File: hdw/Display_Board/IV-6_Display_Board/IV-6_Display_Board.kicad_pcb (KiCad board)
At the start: 4 copper layers, 200 x 50 mm, 238 parts, among them J3001 DSP_IO_Connector, Q1101 PMSTA06, Q1102 BC856W, Q1103 PMSTA06, Q1104 BC856W, Q1105 PMSTA06, Q1106 BC856W, Q1107 PMSTA06, Q1108 BC856W, Q201 PMSTA06, Q202 PMSTA06, Q203 BC856W, Q204 BC856W, Q205 PMSTA06, Q206 PMSTA06, Q207 BC856W, Q208 BC856W, Q209 PMSTA06, Q210 PMSTA06, Q211 BC856W, Q212 BC856W, Q213 PMSTA06, Q214 PMSTA06, Q215 BC856W, Q216 BC856W, Q301 PMSTA06, Q302 PMSTA06, Q303 BC856W, Q304 BC856W, Q305 PMSTA06, Q306 PMSTA06, Q307 BC856W, Q308 BC856W, Q309 PMSTA06, Q310 PMSTA06, Q311 BC856W, Q312 BC856W, SW601 Cap_Touch, SW602 Cap_Touch, SW801 Cap_Touch, SW802 Cap_Touch, SW901 Cap_Touch, U1001 MCP9804, U1301 DS1683, U1302 LTC4316DD, U501 TCA9555RGER, U601 TLV71333PDBV, U602 TLV71333PDBV, U603 AT42QT1010-TSHR, U604 AT42QT1010-TSHR, U605 74LVC1G97, U606 74LVC1G97, U801 TLV71333PDBV, U802 TLV71333PDBV, U803 AT42QT1010-TSHR, U804 AT42QT1010-TSHR, U805 74LVC1G97, U806 74LVC1G97, U901 TLV71333PDBV, U902 AT42QT1010-TSHR, U903 74LVC1G97

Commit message: refactored a lot of display board stuff
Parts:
- Q1101, Q1102, Q1103, Q1104, Q1105, Q1106, Q1107, Q1108, Q301, Q302, Q303, Q304, Q305, Q306, Q307, Q308, Q309, Q310, Q311, Q312, R1101, R1102, R1103, R1104, R1105, R1106, R1107, R1108, R1109, R1110, R1111, R1112, R1113, R1114, R1115, R1116, R1117, R1118, R1119, R1120, R1121, R1122, R1123, R1124, R301, R302, R303, R304, R305, R306, R307, R308, R309, R310, R311, R312, R313, R314, R315, R316, R317, R318, R319, R320, R321, R322, R323, R324: moved to B.Cu
- R501, R502, R503, R504, R505, R506, R507, R508, R509, R510, R511: moved to F.Cu
- moved R229 122.8 mm to (227.4, 74.4), turned to 90 degrees
- moved Q214 119.9 mm to (224.8, 69.7), turned to 270 degrees
- moved R230 118.6 mm to (224.8, 72.2), turned to 180 degrees
- moved Q216 117.7 mm to (224.8, 74.4), turned to 180 degrees
- moved R226 116.0 mm to (222.6, 69.2), turned to 270 degrees
- moved R232 113.7 mm to (222.2, 72.2), turned to 90 degrees
- moved R221 108.2 mm to (220.1, 74.4), turned to 90 degrees
- moved C1301 106.6 mm to (280.2, 106.2)
- moved C1302 106.6 mm to (281.6, 106.2)
- moved C1303 106.6 mm to (283.0, 106.2)
- moved C1304 106.6 mm to (278.8, 106.2)
- moved C1305 106.6 mm to (287.4, 103.4)
- moved D1301 106.6 mm to (286.2, 106.9)
- moved R1303 106.6 mm to (287.4, 104.9)
- moved R1304 106.6 mm to (287.4, 103.4)
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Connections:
- Q203 pad 3: Anode_A_VFD -> Anode_G_VFD
- Q204 pad 3: Anode_E_VFD -> Anode_D_VFD
- Q207 pad 3: Anode_B_VFD -> Anode_E_VFD
- Q208 pad 3: Anode_F_VFD -> Anode_C_VFD
- Q211 pad 3: Anode_C_VFD -> Anode_DP_VFD
- Q212 pad 3: Anode_G_VFD -> Anode_B_VFD
- Q215 pad 3: Anode_D_VFD -> Anode_F_VFD
- Q216 pad 3: Anode_DP_VFD -> Anode_A_VFD
- R201 pad 1: Anode_A_DSP -> Anode_G_DSP
- R202 pad 1: Anode_E_DSP -> Anode_D_DSP
- R207 pad 1: Anode_A_VFD -> Anode_G_VFD
- R208 pad 1: Anode_E_VFD -> Anode_D_VFD
- R209 pad 1: Anode_B_DSP -> Anode_E_DSP
- R210 pad 1: Anode_F_DSP -> Anode_C_DSP
- R215 pad 1: Anode_B_VFD -> Anode_E_VFD
- R216 pad 1: Anode_F_VFD -> Anode_C_VFD
- R217 pad 1: Anode_C_DSP -> Anode_DP_DSP
- R218 pad 1: Anode_G_DSP -> Anode_B_DSP
- R223 pad 1: Anode_C_VFD -> Anode_DP_VFD
- R224 pad 1: Anode_G_VFD -> Anode_B_VFD
- R225 pad 1: Anode_D_DSP -> Anode_F_DSP
- R226 pad 1: Anode_DP_DSP -> Anode_A_DSP
- R231 pad 1: Anode_D_VFD -> Anode_F_VFD
- R232 pad 1: Anode_DP_VFD -> Anode_A_VFD
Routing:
- net Cap_Touch_Up_DSP: track 202.2 -> 0.00 mm, vias 8 -> 0
- net Grid_5_DSP: track 187.8 -> 0.00 mm, vias 3 -> 0
- net Cap_Touch_Down_DSP: track 181.4 -> 0.00 mm, vias 6 -> 0
- net Grid_4_DSP: track 165.4 -> 0.00 mm, vias 3 -> 0
- net Colon_0_DSP: track 153.5 -> 0.00 mm, vias 3 -> 0
- net Colon_1_DSP: track 131.2 -> 0.00 mm, vias 3 -> 0
- net Cap_Touch_Left_DSP: track 130.7 -> 0.00 mm, vias 4 -> 0
- net I2C_DSP_SCL: track 129.7 -> 0.00 mm, vias 3 -> 0
- net Grid_3_DSP: track 119.1 -> 0.00 mm, vias 3 -> 0
- net Cap_Touch_Right_DSP: track 111.8 -> 0.00 mm, vias 2 -> 0
- net Grid_2_DSP: track 96.5 -> 0.00 mm, vias 3 -> 0
- net I2C_DSP_SDA: track 90.1 -> 0.00 mm, vias 1 -> 0
- net Colon_2_DSP: track 87.7 -> 0.00 mm, vias 3 -> 0
- net Anode_B_DSP: track 102.3 -> 27.8 mm, vias 4 -> 2
- net Anode_A_DSP: track 89.8 -> 21.1 mm, vias 4 -> 2
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
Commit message: More display board fixes
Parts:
- added G***: LOGO, Custom Footprints Library:VFD_QR_Code, F.Cu at (139.6, 51.9)
- added G***: LOGO, Custom Footprints Library:VFD_CLock_Logo_Silk, F.Cu at (134.5, 70.4)
- moved U1001 98.5 mm to (197.8, 132.0), turned to 180 degrees
- moved C1001 98.0 mm to (197.8, 134.2), turned to 0 degrees
- moved U1302 69.6 mm to (221.9, 123.5), turned to 180 degrees
- moved C1305 65.5 mm to (225.0, 123.5), turned to 270 degrees
- moved R1304 65.5 mm to (225.0, 123.5), turned to 270 degrees
- moved R1303 63.6 mm to (226.6, 123.5), turned to 90 degrees
- moved D1301 60.3 mm to (228.6, 124.7), turned to 90 degrees
- moved U1301 60.2 mm to (226.6, 129.2), turned to 270 degrees
- moved R1301 60.0 mm to (225.2, 133.8), turned to 180 degrees
- moved C1303 59.3 mm to (227.8, 127.9), turned to 180 degrees
- moved C1302 58.5 mm to (227.8, 129.3), turned to 180 degrees
- moved C1301 57.8 mm to (227.8, 130.7), turned to 180 degrees
- moved R1302 57.8 mm to (226.9, 133.8), turned to 180 degrees
- moved C1304 57.2 mm to (227.8, 132.1), turned to 180 degrees
- moved Q306 2.45 mm to (200.7, 94.8)
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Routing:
- net Grid_0_DSP: track 0.00 -> 27.5 mm, vias 0 -> 2
- net Grid_1_DSP: track 0.00 -> 26.6 mm, vias 0 -> 2
- net Grid_2_DSP: track 0.00 -> 25.7 mm, vias 0 -> 2
- net Grid_3_DSP: track 0.00 -> 24.8 mm, vias 0 -> 2
- net Grid_4_DSP: track 0.00 -> 23.9 mm, vias 0 -> 2
- net Grid_5_DSP: track 0.00 -> 23.1 mm, vias 0 -> 2
- net Colon_0_DSP: track 0.00 -> 22.2 mm, vias 0 -> 2
- net Colon_1_DSP: track 0.00 -> 21.3 mm, vias 0 -> 2
- net Colon_2_DSP: track 0.00 -> 20.6 mm, vias 0 -> 2
- net Colon_3_DSP: track 0.00 -> 20.0 mm, vias 0 -> 2
- net Net-(Q306-Pad3): track 1.85 -> 3.79 mm

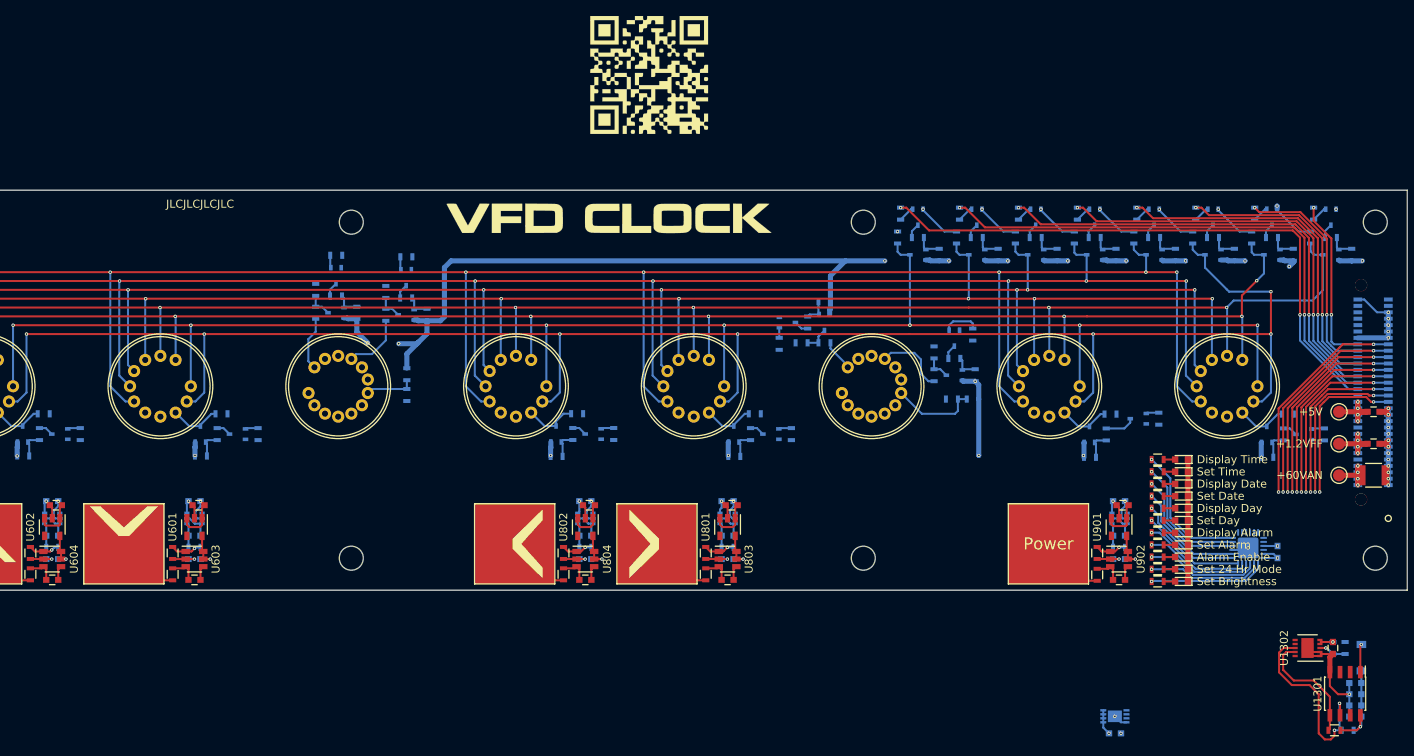
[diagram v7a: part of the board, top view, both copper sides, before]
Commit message: reclassed some nets, placed I2C devices
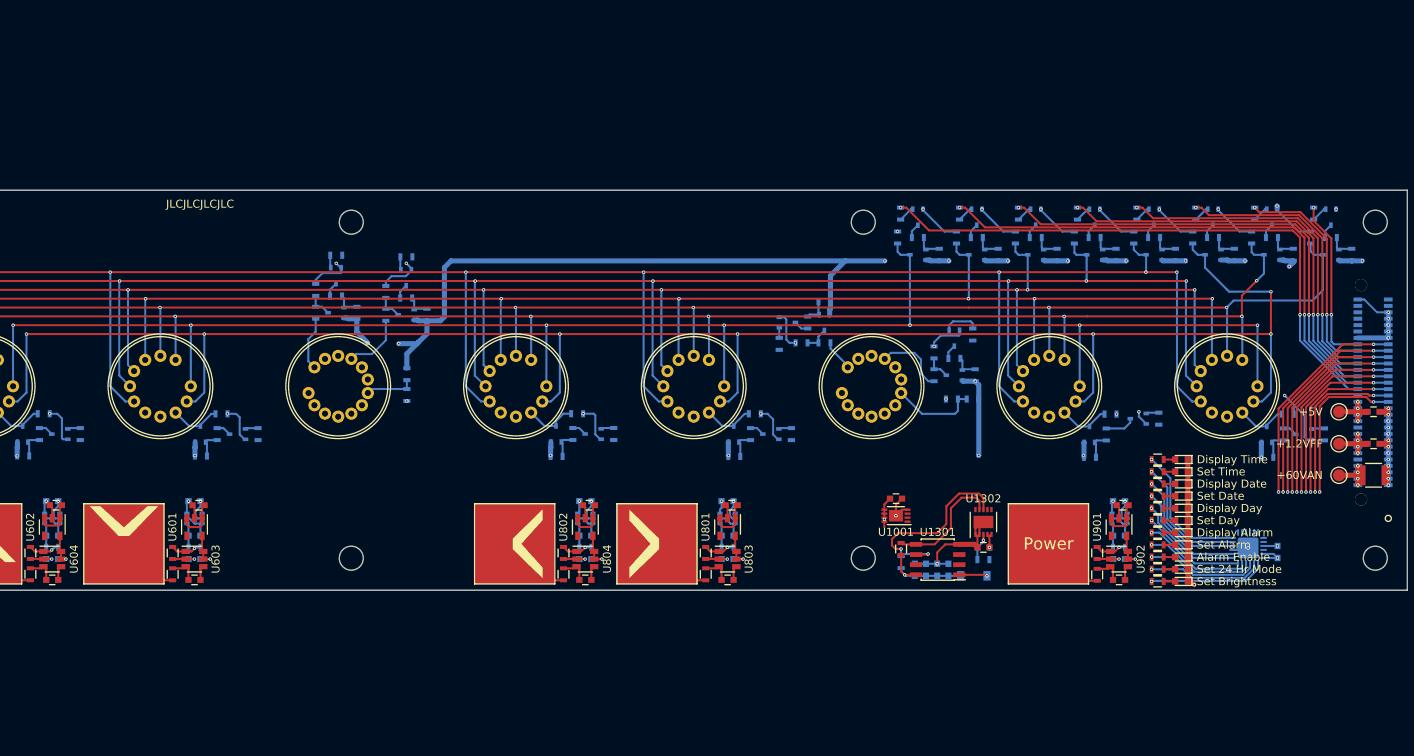
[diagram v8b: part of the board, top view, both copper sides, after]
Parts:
- removed G***: LOGO, Custom Footprints Library:VFD_QR_Code
- removed G***: LOGO, Custom Footprints Library:VFD_CLock_Logo_Silk
- C1001, U1001: moved to F.Cu
- moved R1302 59.6 mm to (171.1, 112.8), turned to 90 degrees
- moved R1301 58.7 mm to (171.1, 111.1), turned to 90 degrees
- moved C1304 58.0 mm to (172.8, 113.7), turned to 90 degrees
- moved C1301 56.3 mm to (174.2, 113.7), turned to 90 degrees
- moved C1302 54.5 mm to (175.6, 113.7), turned to 90 degrees
- moved U1301 53.6 mm to (175.6, 112.5), turned to 180 degrees
- moved C1303 52.8 mm to (177.0, 113.7), turned to 90 degrees
- moved D1301 49.5 mm to (180.1, 114.5), turned to 0 degrees
- moved R1303 46.5 mm to (181.4, 112.5), turned to 0 degrees
- moved C1305 45.5 mm to (181.4, 110.9), turned to 180 degrees
- moved R1304 45.5 mm to (181.4, 110.9), turned to 180 degrees
- moved U1302 43.5 mm to (181.4, 107.8), turned to 90 degrees
- moved C1001 40.1 mm to (170.4, 104.8)
- moved U1001 37.1 mm to (170.4, 107.0)
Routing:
- net GND: track 165.7 -> 219.5 mm, vias 42 -> 55
- net +5V: track 67.4 -> 68.0 mm
